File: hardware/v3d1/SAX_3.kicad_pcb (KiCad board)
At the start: 2 copper layers, 86 parts, among them J1 joystick, J2 LED strip, J3 SSD1306 SPI, J4 Midi Y:M5 - R:M4, J5 Batt, J6 Beak - R BK Y, J7 Conn_01x03_Female, J8 MXP5010, U1 74HC165, U2 74HC165, U3 74HC165, U4 Teensy3.2_breadboard_friendly

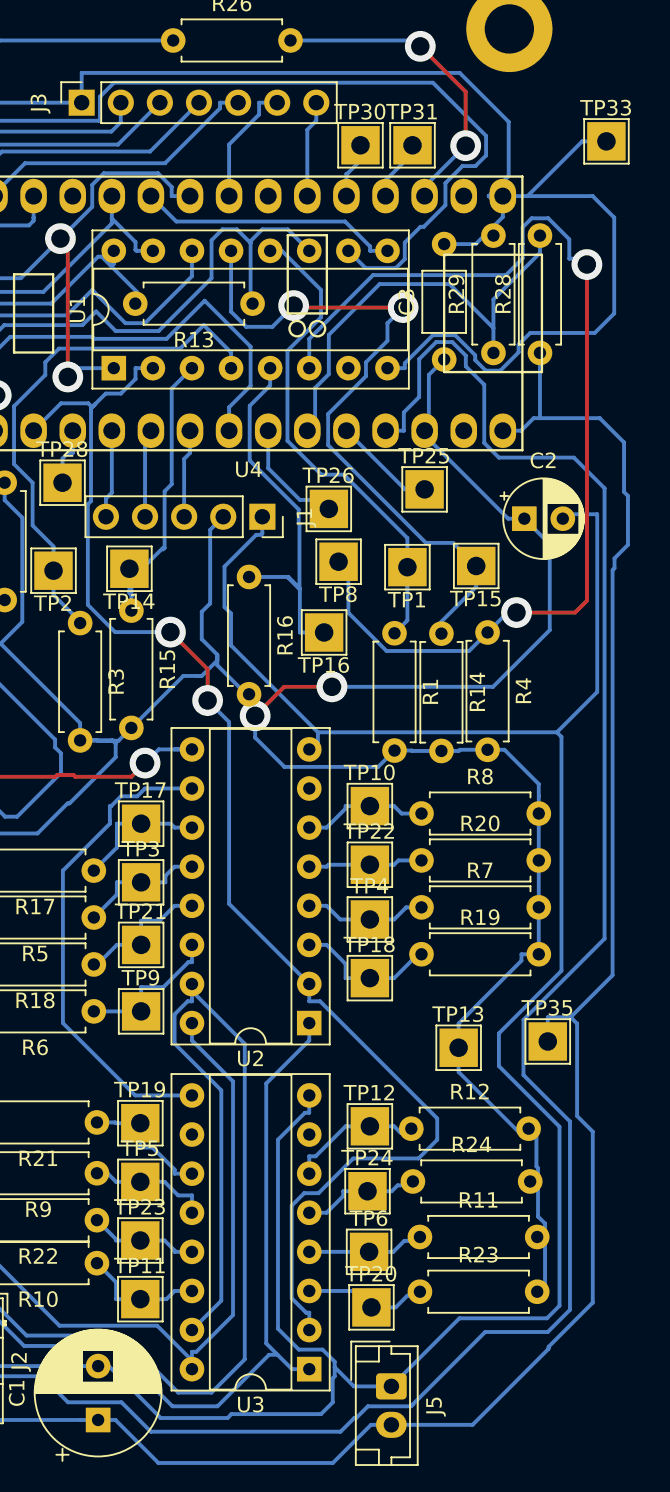
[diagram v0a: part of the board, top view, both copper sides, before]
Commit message: Migrated to kicad v6
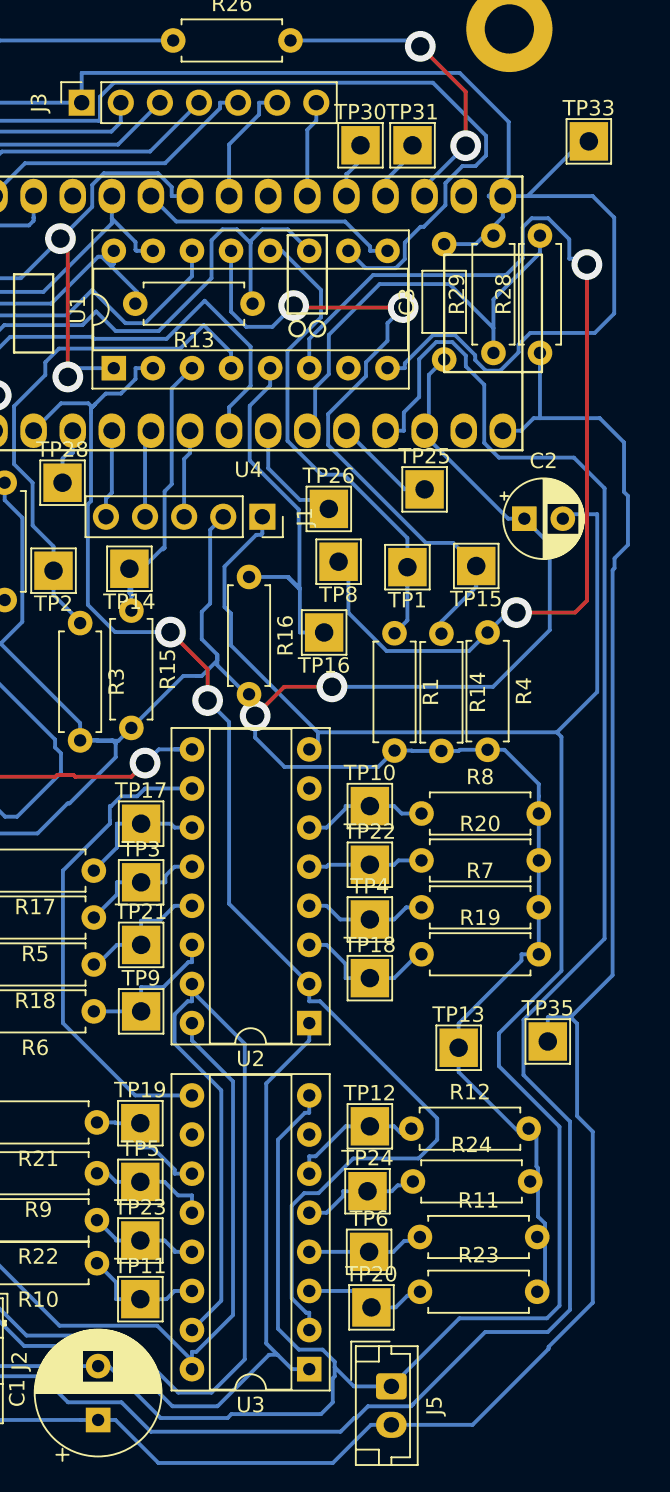
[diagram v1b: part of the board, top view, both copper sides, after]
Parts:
- moved TP33 1.14 mm to (254.6, 28.7)
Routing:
- net GND: track 355.1 -> 354.0 mm
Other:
- net class Default removed
- net class Power Strip removed

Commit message: update
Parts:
- moved TP34 0.99 mm to (205.1, 63.0)
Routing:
- net GND: track 354.0 -> 352.8 mm
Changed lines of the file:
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@@
   )
   (setup
+    (stackup
+      (layer "F.SilkS" (type "Top Silk Screen"))
+      (layer "F.Paste" (type "Top Solder Paste"))
+      (layer "F.Mask" (type "Top Solder Mask") (thickness 0.01))
+      (layer "F.Cu" (type "copper") (thickness 0.035))
+      (layer "dielectric 1" (type "core") (thickness 1.51) (material "FR4") (epsilon_r 4.5) (loss_tangent 0.02))
+      (layer "B.Cu" (type "copper") (thickness 0.035))
+      (layer "B.Mask" (type "Bottom Solder Mask") (thickness 0.01))
+      (layer "B.Paste" (type "Bottom Solder Paste"))
+      (layer "B.SilkS" (type "Bottom Silk Screen"))
+      (copper_finish "None")
+      (dielectric_constraints no)
+    )
     (pad_to_mask_clearance 0.051)
     (solder_mask_min_width 0.25)
@@
   )
   (footprint "TestPoint:TestPoint_THTPad_2.5x2.5mm_Drill1.2mm" (layer "F.Cu")
-    (at 205.74 63.754)
+    (at 205.105 62.992)
     (descr "THT rectangular pad as test Point, square 2.5mm side length, hole diameter 1.2mm")
     (tags "test point THT pad rectangle square")
@@
   (segment (start 247.2542 42.9124) (end 247.2542 42.594) (width 0.25) (layer "B.Cu") (net 1))
   (segment (start 211.60001 90.4154) (end 211.60001 90.428008) (width 0.25) (layer "B.Cu") (net 1))
-  (segment (start 206.629 64.77) (end 205.8105 63.9515) (width 0.25) (layer "B.Cu") (net 1))
   (segment (start 234.442 105.83355) (end 235.79645 107.188) (width 0.25) (layer "B.Cu") (net 1))
   (segment (start 244.5036 41.2913) (end 242.6793 43.1156) (width 0.25) (layer "B.Cu") (net 1))
@@
   (segment (start 247.8417 48.2919) (end 247.8417 44.5123) (width 0.25) (layer "B.Cu") (net 5))
   (segment (start 240.284 110.871) (end 243.08501 110.871) (width 0.25) (layer "B.Cu") (net 5))
-  (segment (start 207.9496 102.7139) (end 208.12935 102.89365) (width 0.25) (layer "B.Cu") (net 5))
   (segment (start 239.522 111.633) (end 240.284 110.871) (width 0.25) (layer "B.Cu") (net 5))
   (segment (start 214.1537 108.918) (end 219.109 108.918) (width 0.25) (layer "B.Cu") (net 5))

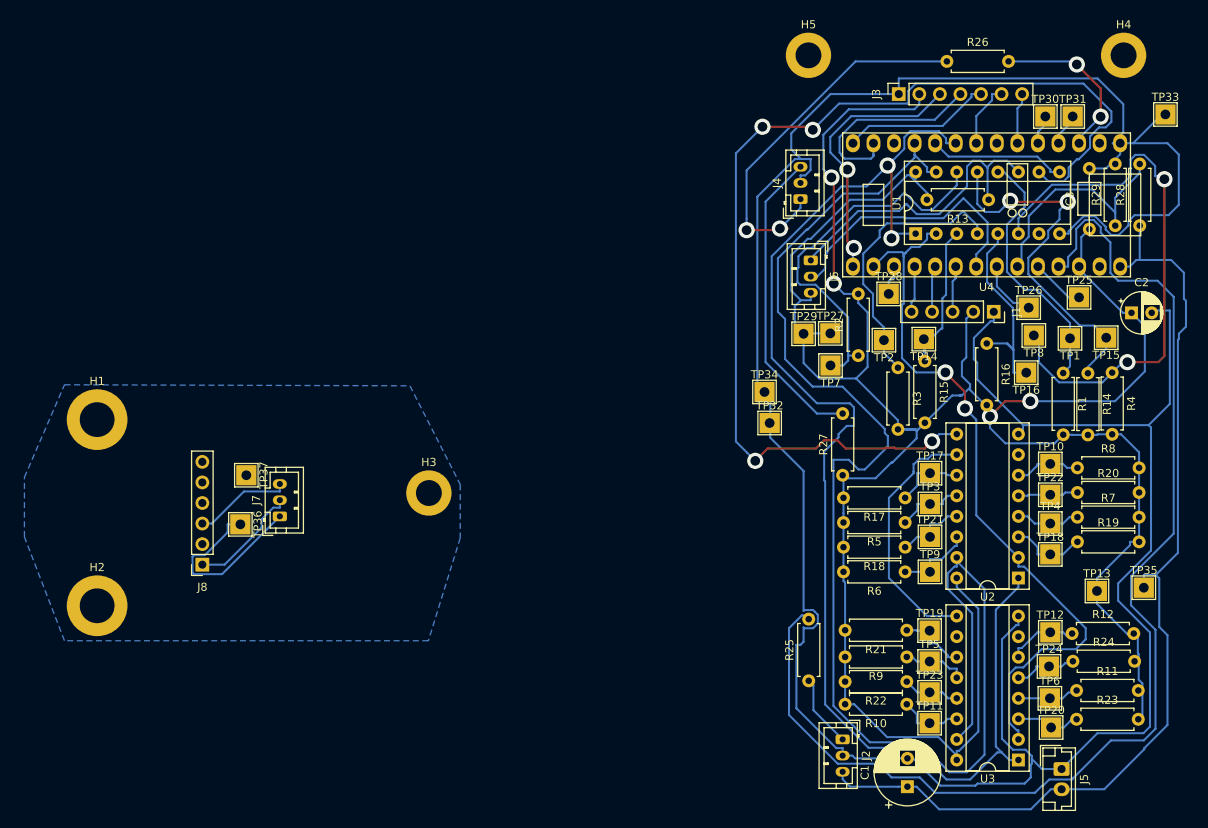
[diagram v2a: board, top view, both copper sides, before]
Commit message: Fixed drift in analogInput
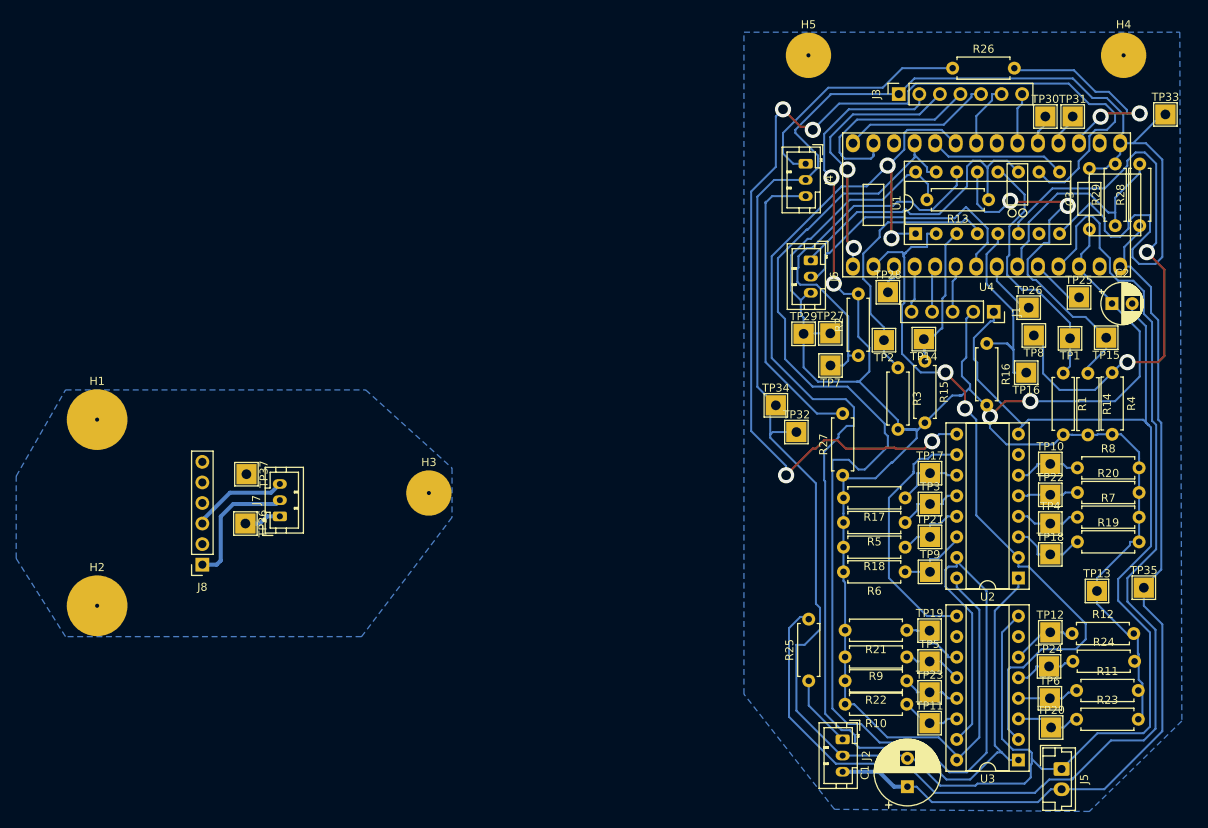
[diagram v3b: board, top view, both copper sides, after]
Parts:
- J1: value joystick -> J - 3.3 G
- J3: value SSD1306 SPI -> SSD1306 G 3.3
- J4: value Midi Y:M5 - R:M4 -> Midi M4 M2 M5
- U4: value Teensy3.2_breadboard_friendly -> Teensy3.2 - USB ->
- moved J4 4.41 mm to (210.2, 34.8), turned to -90 degrees
- moved TP32 3.49 mm to (209.0, 67.9)
- moved C2 2.67 mm to (248.0, 52.1)
- moved TP34 2.16 mm to (206.5, 64.6)
- moved R26 1.10 mm to (228.3, 23.0)
- moved TP36 0.63 mm to (141.0, 79.2)
- moved TP28 0.23 mm to (220.3, 50.7)
- moved TP37 0.13 mm to (141.1, 73.2)
- moved R22 0.10 mm to (222.7, 98.7)
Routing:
- net Net-(J7-Pad1): track 24.0 -> 4.62 mm
- net Net-(J4-Pad1): track 47.6 -> 30.3 mm, vias 2 -> 0
- net +5V: track 121.3 -> 112.8 mm
- net Net-(R26-Pad2): track 20.9 -> 27.4 mm
- net GND: track 352.8 -> 359.1 mm
- net Net-(R25-Pad2): track 149.0 -> 145.5 mm
- net Net-(J7-Pad2): track 14.0 -> 16.1 mm
- net /SR_CLK_INH: track 171.0 -> 172.6 mm
- net /SR_SH: track 160.0 -> 161.5 mm
- net Net-(J6-Pad2): track 34.4 -> 32.9 mm
- net Net-(U1-Pad10): track 135.1 -> 136.3 mm
- net Net-(R4-Pad1): track 69.6 -> 70.8 mm
- net Net-(R3-Pad1): track 34.4 -> 33.3 mm
- net /SR_CLK: track 90.2 -> 91.2 mm
- net Net-(R2-Pad1): track 47.0 -> 46.1 mm
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- added copper zone on B.Cu, net GND
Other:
- board text added: "TES sax v3.1 SPI SSD1306 LED strip"
- board text removed: "TES sax v3 SPI SSD1306 LED strip"
